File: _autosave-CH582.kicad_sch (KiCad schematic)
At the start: 52 parts, among them J1 Conn_01x02, J2 Conn_01x02, J3 Peripherals, J4 USB, SW2 POWER, U2 XC6220B331QR-G, U3 M3406, U4 TP4056, Y1 32MHz, Y2 Crystal_Small

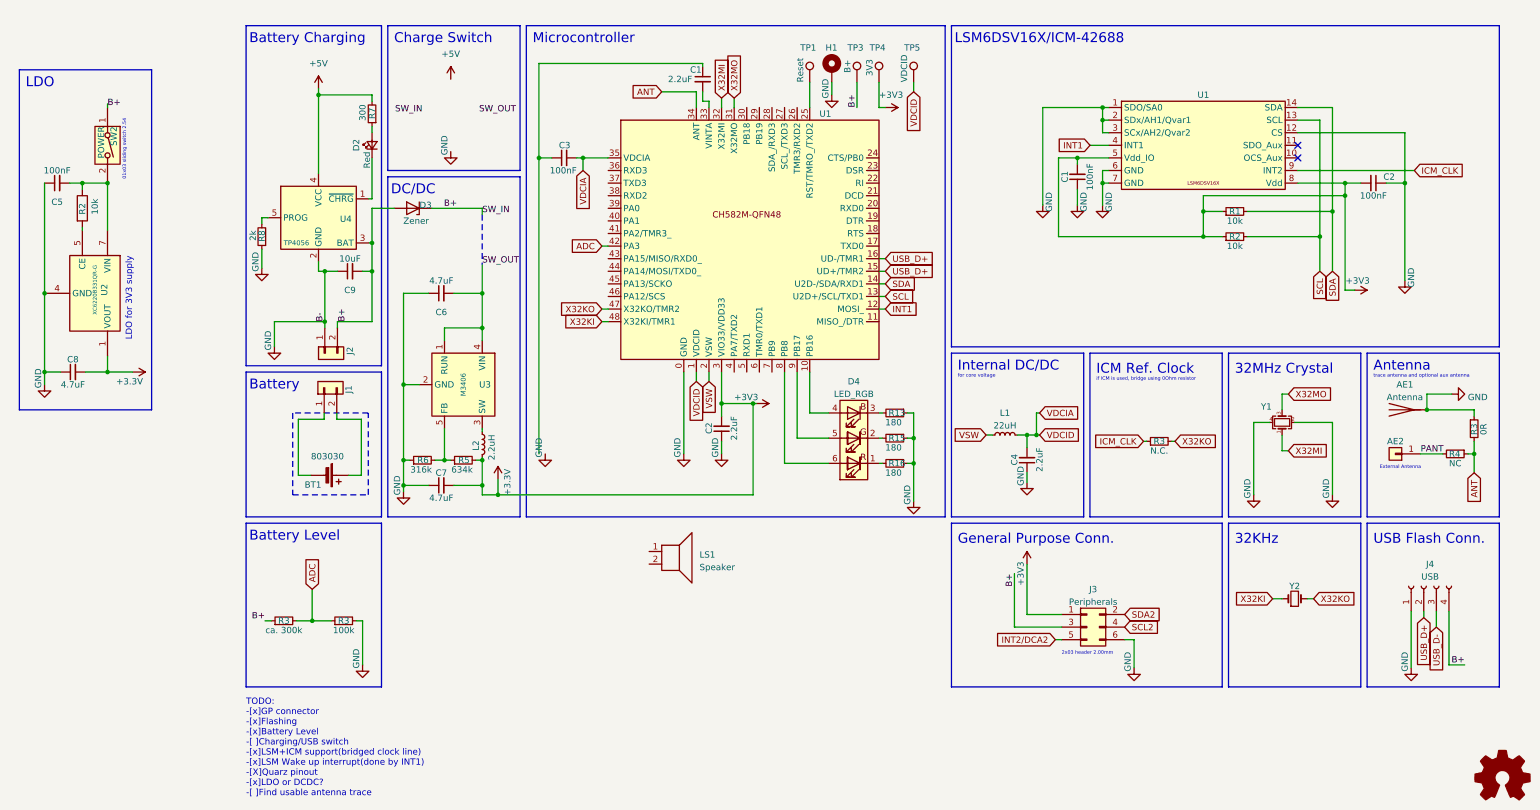
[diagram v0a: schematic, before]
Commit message: added pogo port and reset switch
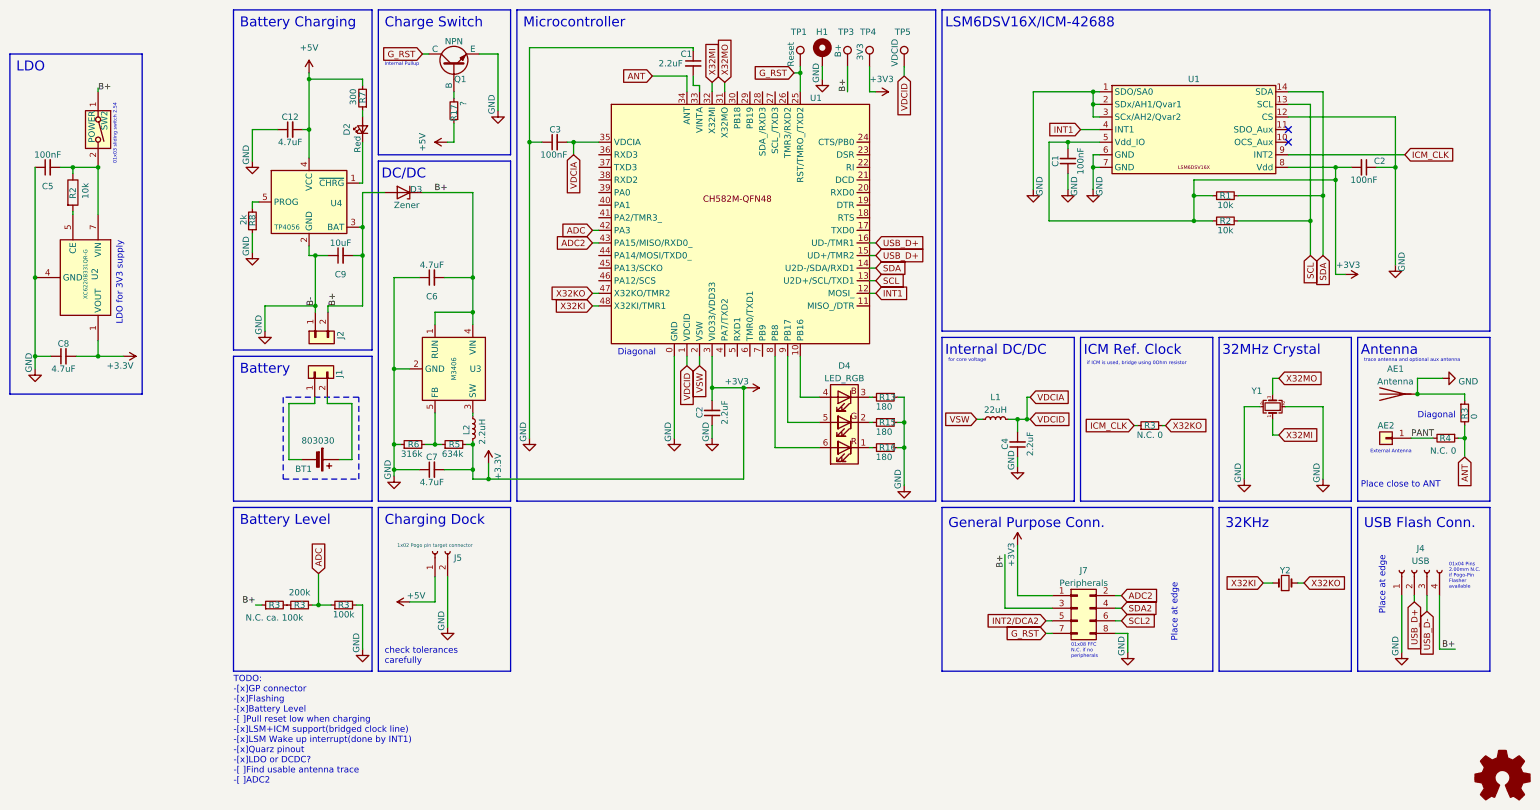
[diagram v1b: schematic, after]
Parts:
- removed J3: Peripherals, symbol Connector_Generic:Conn_02x03_Odd_Even
- removed LS1: Speaker, symbol Device:Speaker
- added C12: 4.7uF, Capacitor_SMD:C_1206_3216Metric_Pad1.33x1.80mm_HandSolder, symbol Device:C_Small
- added J5: 1x02 Pogo pin target connector, symbol Connector:Conn_01x02_Socket
- added J7: Peripherals, symbol Connector_Generic:Conn_02x04_Odd_Even
- added Q1: NPN, symbol Simulation_SPICE:NPN
- added R17: ?, symbol Device:R_Small
- added R3: 200k, Resistor_SMD:R_0805_2012Metric_Pad1.20x1.40mm_HandSolder, symbol Device:R_Small
- R3: value ca. 300k -> N.C. ca. 100k
- R3: value N.C. -> N.C. 0
- R3: value 0R -> 0
- R4: value NC -> N.C. 0
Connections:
- net SW_OUT is gone; now on net B+: C6.2, U3.1 (RUN), U3.4 (VIN)
- net +3V3: now also J7.1 (Pin_1)
- net +5V: now also C12.2, J5.1 (Pin_1), R17.1
- net ADC: now also R3.2; no longer R3.2
- net B+: now also J7.3 (Pin_3)
- net GND: now also C1.1, C3.1, C12.1, J5.2 (Pin_2), J7.8 (Pin_8), Q1.3 (E)
- net INT2/DCA2: now also J7.5 (Pin_5)
- net SCL2: now also J7.6 (Pin_6)
- net SDA2: now also J7.4 (Pin_4)
- net G_RST: now reaches TP1.1, U1.25 (RST/TMRO_/TXD2)
- net G_RST: now also J7.7 (Pin_7), Q1.1 (C)
- net ADC2: now reaches U1.43 (PA15/MISO/RXD0_)
- net ADC2: now also J7.2 (Pin_2)
- new net: R3.1, R3.2
- new net: Q1.2 (B), R17.2
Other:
- note added: "01x04 Pins 2.00mm N.C. if Pogo-Pin Flasher available"
- note added: "01x08 FFC N.C. if no peripherals"
- note added: "Charging Dock"
- note added: "Diagonal"
- note added: "Internal Pullup"
- note added: "Place at edge"
- note added: "Place close to ANT"
- note added: "TODO: -[x]GP connector -[x]Flashing -[x]Battery Level -[ ]Pull reset low when charging -[x]LSM+ICM support(bridged clock line) -[x]LSM Wake up interrupt(done by INT1) -[x]Quarz pinout -[x]LDO or DCDC? -[ ]Find usable antenna trace -[ ]ADC2"
- note added: "check tolerances carefully"
- note removed: "2x03 header 2.00mm"
- note removed: "TODO: -[x]GP connector -[x]Flashing -[x]Battery Level -[ ]Charging/USB switch -[x]LSM+ICM support(bridged clock line) -[x]LSM Wake up interrupt(done by INT1) -[X]Quarz pinout -[x]LDO or DCDC? -[ ]Find usable antenna trace"
- moved on the sheet: AE1, AE2, BT1, C1, C2, C3, C4, C5, C6, C7, C8, C9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
